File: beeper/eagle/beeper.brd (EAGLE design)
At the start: 27.6 x 41.9 mm, 32 parts, among them Q1 16MHz, T1 3904, U1 ATMEGA328P, U2 ATA6631

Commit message: Minor board tweaks. Work in progress.
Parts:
- moved R8 13.3 mm to (15.4, 10.7), turned to 180 degrees
- moved C4 13.3 mm to (24.7, 13.4), turned to 0 degrees
- moved T1 12.7 mm to (15.8, 6.73)
- moved C7 12.0 mm to (11.4, 18.4), turned to 90 degrees
- moved R1 7.54 mm to (19.6, 13.3)
- moved R10 6.35 mm to (15.2, 26.7)
- moved D1 6.29 mm to (15.7, 2.62), turned to 0 degrees
- moved C8 5.09 mm to (14.8, 21.2), turned to 270 degrees
- moved LED3 3.81 mm to (20.3, 3.81)
- moved R6 3.59 mm to (20.3, 32.4)
- moved R7 3.59 mm to (17.8, 32.4)
- moved U1 3.06 mm to (21.8, 20.4)
- moved U2 2.72 mm to (5.38, 17.8)
- moved C3 2.58 mm to (3.35, 22.9)
- moved JP2 2.54 mm to (24.1, 30.5), turned to 270 degrees
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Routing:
- net GND: track 0.00 -> 7.18 mm
- net N$1: track 0.00 -> 2.94 mm
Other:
- board size 27.6 x 41.9 mm -> 27.9 x 39.8 mm

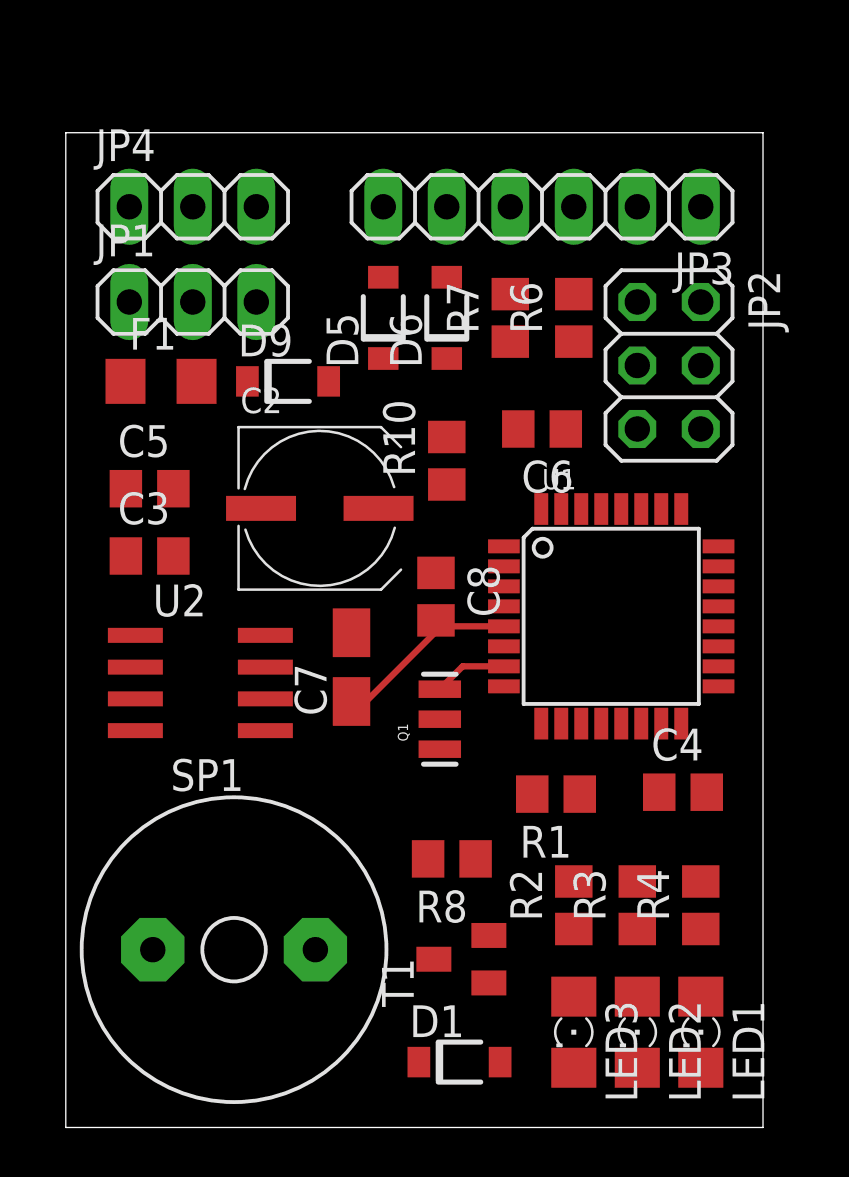
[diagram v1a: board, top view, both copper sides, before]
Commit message: First complete routing. Still needs TLC.
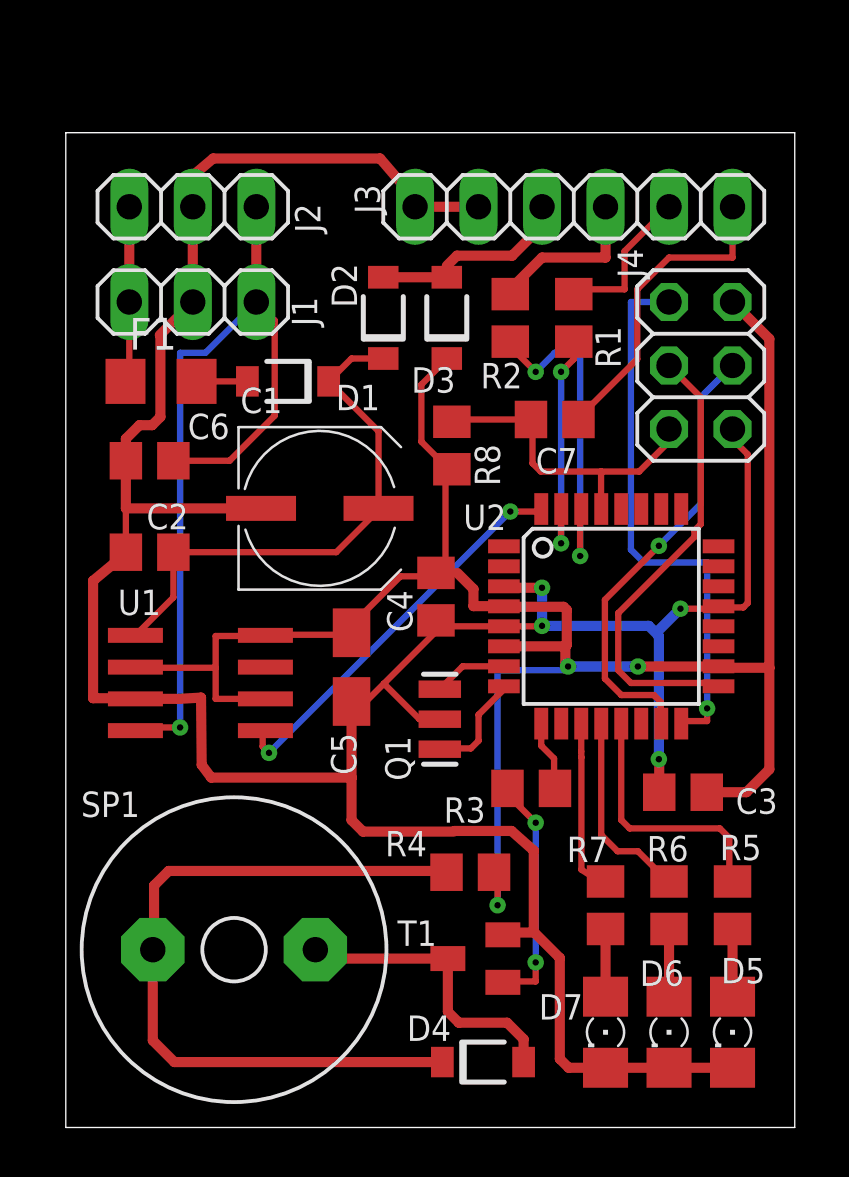
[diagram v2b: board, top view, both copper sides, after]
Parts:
- removed C8: 0.1uF, rcl:C0805
- removed D9: MBR0540, diode:SOD123FL
- removed JP2: ICSP, pinhead:2X03
- removed JP3: (no value), pinhead:1X06
- removed LED1, LED2: GREEN, led:1206
- removed LED3: RED, led:1206
- removed R10: 10k, rcl:R0805
- added C1: 22uF, rcl:UD-6,3X5,8_NICHICON
- added D2, D3: MBR0540, diode:SOD123FL
- added D4: MBR0560, diode:SOD123FL
- added D7: GREEN, led:1206
- added J3: (no value), pinhead:1X06
- added J4: ICSP, pinhead:2X03
- added R5: 3.3K, rcl:R0805
- C2: value 22uF -> 0.1uF; device rcl:UD-6,3X5,8_NICHICON -> rcl:C0805
- C3: value 220pF -> 0.1uF
- C5: value 0.1uF -> 10uF; device rcl:C0805 -> rcl:A/3216-18R
- C6: value 0.01uF -> 220pF
- C7: value 10uF -> 0.01uF; device rcl:A/3216-18R -> rcl:C0805
- D1: value MBR0560 -> MBR0540
- D5: value MBR0540 -> RED; device diode:SOD123FL -> led:1206
- D6: value MBR0540 -> GREEN; device diode:SOD123FL -> led:1206
- R1: value 5K -> 10k
- R2: value 3.3K -> 10k
- R3: value 470 -> 5K
- R4: value 470 -> 220
- R6, R7: value 10k -> 470
- R8: value 220 -> 10k
- U1: value ATMEGA328P -> ATA6631; device beeper:TQFP32-08 -> beeper:SO-08
- U2: value ATA6631 -> ATMEGA328P; device beeper:SO-08 -> beeper:TQFP32-08
- moved D5 31.8 mm to (26.7, 3.81), turned to 270 degrees
- moved D6 29.9 mm to (24.1, 3.81), turned to 270 degrees
- moved D1 28.1 mm to (8.89, 29.8), turned to 180 degrees
- moved R6 23.8 mm to (24.1, 8.89)
- moved R7 23.8 mm to (21.6, 8.89)
- moved R2 23.6 mm to (17.8, 32.4)
- moved C3 23.3 mm to (24.7, 13.4), turned to 180 degrees
- moved R1 19.1 mm to (20.3, 32.4), turned to 90 degrees
- moved U1 16.6 mm to (5.38, 17.8), turned to 270 degrees
- moved U2 16.6 mm to (21.8, 20.4), turned to 0 degrees
- moved R8 16.5 mm to (15.4, 27.3), turned to 270 degrees
- moved C6 15.7 mm to (3.35, 26.7)
- moved C7 12.8 mm to (19.6, 28.3), turned to 180 degrees
- moved C4 12.6 mm to (14.8, 21.2), turned to 270 degrees
- moved C5 10.8 mm to (11.4, 18.4), turned to 90 degrees
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- renumbered JP1 to J1, JP4 to J2
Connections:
- removed net N$1: Q1.3, U1.7
- removed net N$11: Q1.1, U1.8
- new net XTAL1: Q1.3, U2.7
- new net XTAL2: Q1.1, U2.8
- net +12V: now also C1.+, C2.1, D1.C, D2.C, U1.1; no longer C2.+, C5.1, D5.C, D9.C, U2.1
- net +5V: now also C3.1, C5.+, D3.C, J4.2, R4.2, U1.2, U1.8, U2.18, U2.4; no longer C7.+, C8.1, D6.C, JP2.2, R10.2, U1.18, U1.4, U2.2, U2.8
- net DTR: now also C7.1, J3.1; no longer C6.1, JP3.1
- net GND: now also C1.-, C2.2, C5.-, C6.2, D5.C, D6.C, D7.C, J3.5, J3.6, J4.6, U2.21, U2.5; no longer C2.-, C5.2, C7.-, C8.2, JP2.6, JP3.5, JP3.6, LED1.C, LED2.C, LED3.C, U1.21, U1.5
- net LIN: now also C6.1, U1.4; no longer C3.1, U2.4
- net LIN_RX: now also U1.5, U2.32; no longer U1.32, U2.5
- net N$14: now also R2.1, U2.30; no longer R7.1, U1.30
- net N$15: now also C7.2, J4.5, R8.1, U2.29; no longer C6.2, JP2.5, R10.1, U1.29
- net N$17: now also R3.1, U2.9; no longer R1.1, U1.9
- net N$19: now also R3.2; no longer R1.2
- net N$2: now also D7.A, R7.1; no longer LED1.A, R4.1
- net N$20: now also J4.4, U2.15; no longer JP2.4, U1.15
- net N$22: now also R1.1, U2.31; no longer R6.1, U1.31
- net N$25: now also J4.1, U2.16; no longer JP2.1, U1.16
- net N$28: now also J4.3, U2.17; no longer JP2.3, U1.17
- net N$3: now also D6.A, R6.1; no longer LED2.A, R3.1
- net N$30: now also D4.C, R4.1; no longer D1.C, R8.1
- net N$31: now also D4.A; no longer D1.A
- net N$4: now also D5.A, R5.1; no longer LED3.A, R2.1
- net N$6: now also D1.A; no longer D9.A
- net N$7: now also R5.2, U2.13; no longer R2.2, U1.13
- net N$8: now also R6.2, U2.12; no longer R3.2, U1.12
- net N$9: now also R7.2, U2.11; no longer R4.2, U1.11
- net RXI: now also J3.2, R1.2; no longer JP3.2, R6.2
- net S-5V: now also D2.A, D3.A, J3.4; no longer D5.A, D6.A, JP3.4
- net TXO: now also J3.3, R2.2; no longer JP3.3, R7.2
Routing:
- net GND: track 7.18 -> 121.8 mm, vias 0 -> 4
- net +5V: track 0.00 -> 83.5 mm, vias 0 -> 3
- net LIN: track 0.00 -> 34.2 mm, vias 0 -> 1
- net N$30: track 0.00 -> 30.1 mm
- net N$25: track 0.00 -> 22.2 mm, vias 0 -> 1
- net +12V: track 0.00 -> 21.4 mm
- net N$28: track 0.00 -> 18.3 mm
- net N$20: track 0.00 -> 18.1 mm, vias 0 -> 1
- net LIN_RX: track 0.00 -> 15.9 mm, vias 0 -> 2
- net N$14: track 0.00 -> 13.7 mm, vias 0 -> 2
- net N$15: track 0.00 -> 13.1 mm
- net DTR: track 0.00 -> 12.5 mm
- net N$31: track 0.00 -> 12.0 mm
- net N$7: track 0.00 -> 10.3 mm
- net N$22: track 0.00 -> 9.65 mm, vias 0 -> 2
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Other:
- board size 27.9 x 39.8 mm -> 29.2 x 39.8 mm

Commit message: Added heatsink copper below the LDO. General tweaks. Layout is complete. Need to verify and fix DRC's.
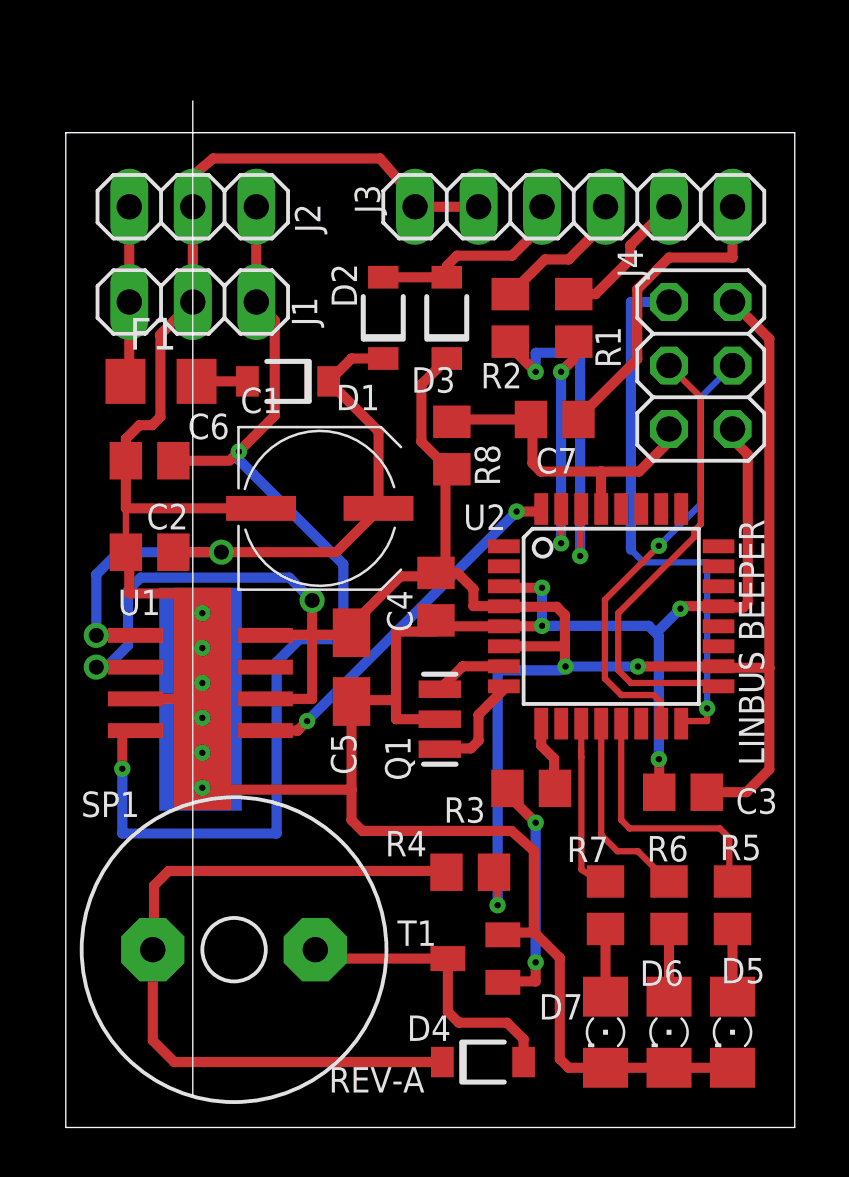
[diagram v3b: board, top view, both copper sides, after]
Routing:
- net N$1: track 0.00 -> 13.7 mm, vias 0 -> 6
- net +5V: track 83.5 -> 93.6 mm, vias 3 -> 5
- net LIN: track 34.2 -> 43.1 mm, vias 1 -> 2
- net +12V: track 21.4 -> 26.8 mm, vias 0 -> 2
- net GND: track 121.8 -> 126.1 mm
- net LIN_RX: track 15.9 -> 14.7 mm
- net TXO: track 6.56 -> 5.63 mm
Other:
- board size 29.2 x 39.8 mm -> 29.2 x 41.1 mm
- board text added: "LINBUS BEEPER"
- board text added: "REV-A"

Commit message: Updated PDF of board top view.
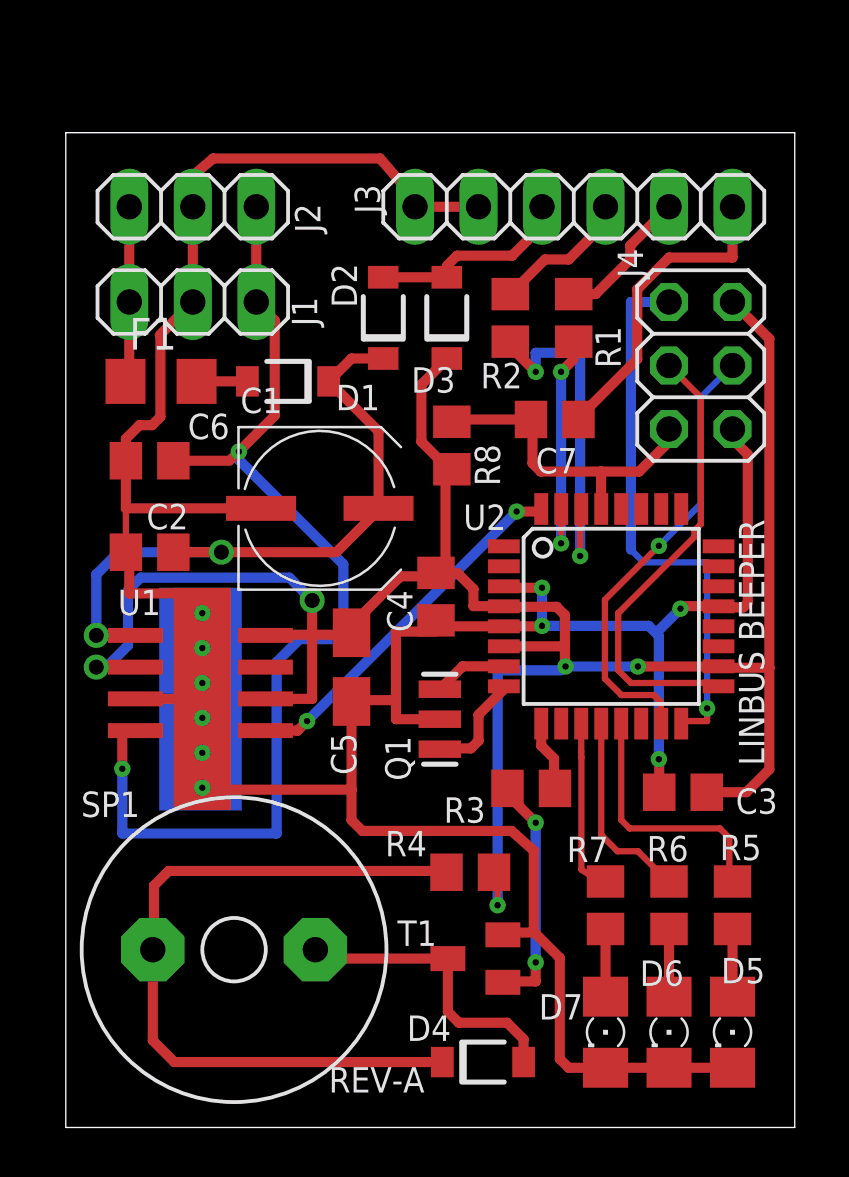
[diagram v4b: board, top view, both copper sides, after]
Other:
- board size 29.2 x 41.1 mm -> 29.2 x 39.8 mm
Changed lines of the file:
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@@
 <layer number="27" name="tValues" color="7" fill="1" visible="yes" active="yes"/>
 <layer number="28" name="bValues" color="7" fill="1" visible="yes" active="yes"/>
-<layer number="29" name="tStop" color="7" fill="3" visible="yes" active="yes"/>
-<layer number="30" name="bStop" color="7" fill="6" visible="yes" active="yes"/>
-<layer number="31" name="tCream" color="7" fill="4" visible="yes" active="yes"/>
-<layer number="32" name="bCream" color="7" fill="5" visible="yes" active="yes"/>
-<layer number="33" name="tFinish" color="6" fill="3" visible="yes" active="yes"/>
-<layer number="34" name="bFinish" color="6" fill="6" visible="yes" active="yes"/>
+<layer number="29" name="tStop" color="7" fill="3" visible="no" active="yes"/>
+<layer number="30" name="bStop" color="7" fill="6" visible="no" active="yes"/>
+<layer number="31" name="tCream" color="7" fill="4" visible="no" active="yes"/>
+<layer number="32" name="bCream" color="7" fill="5" visible="no" active="yes"/>
+<layer number="33" name="tFinish" color="6" fill="3" visible="no" active="yes"/>
+<layer number="34" name="bFinish" color="6" fill="6" visible="no" active="yes"/>
 <layer number="35" name="tGlue" color="7" fill="4" visible="yes" active="yes"/>
 <layer number="36" name="bGlue" color="7" fill="5" visible="yes" active="yes"/>
@@
 <layer number="103" name="tMap" color="7" fill="1" visible="yes" active="yes"/>
 <layer number="104" name="Name" color="7" fill="1" visible="yes" active="yes"/>
-<layer number="105" name="tPlate" color="7" fill="1" visible="yes" active="yes"/>
-<layer number="106" name="bPlate" color="7" fill="1" visible="yes" active="yes"/>
+<layer number="105" name="tPlate" color="7" fill="1" visible="no" active="yes"/>
+<layer number="106" name="bPlate" color="7" fill="1" visible="no" active="yes"/>
 <layer number="107" name="Crop" color="7" fill="1" visible="yes" active="yes"/>
 <layer number="116" name="Patch_BOT" color="9" fill="4" visible="yes" active="yes"/>
@@
 <rectangle x1="4.318" y1="12.7" x2="6.604" y2="21.59" layer="1"/>
 <rectangle x1="3.7338" y1="12.6746" x2="7.0358" y2="21.59" layer="16"/>
-<wire x1="5.08" y1="41.0618" x2="5.08" y2="1.27" width="0" layer="20"/>
 <text x="27.94" y="14.478" size="1.016" layer="21" rot="R90">LINBUS BEEPER</text>
 <text x="14.351" y="2.413" size="1.016" layer="21" rot="R180">REV-A</text>

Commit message: Increased min dril to 12mil to comply with PCB house requirements.
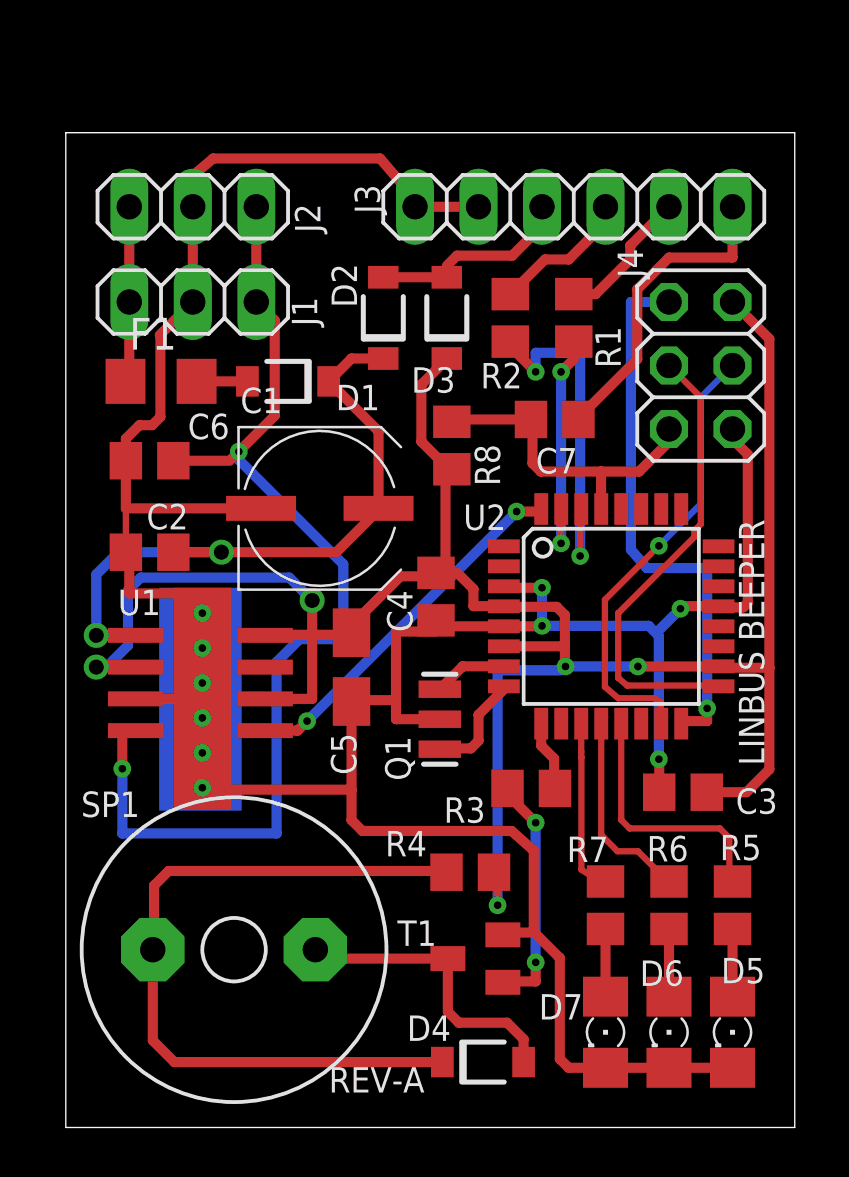
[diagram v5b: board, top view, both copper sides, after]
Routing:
- net N$1: track 13.7 -> 2.77 mm, vias 6 -> 2
- net GND: track 126.1 -> 122.3 mm
- net N$5: track 0.00 -> 1.50 mm, vias 0 -> 2

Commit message: Board layout tweaked and verified.
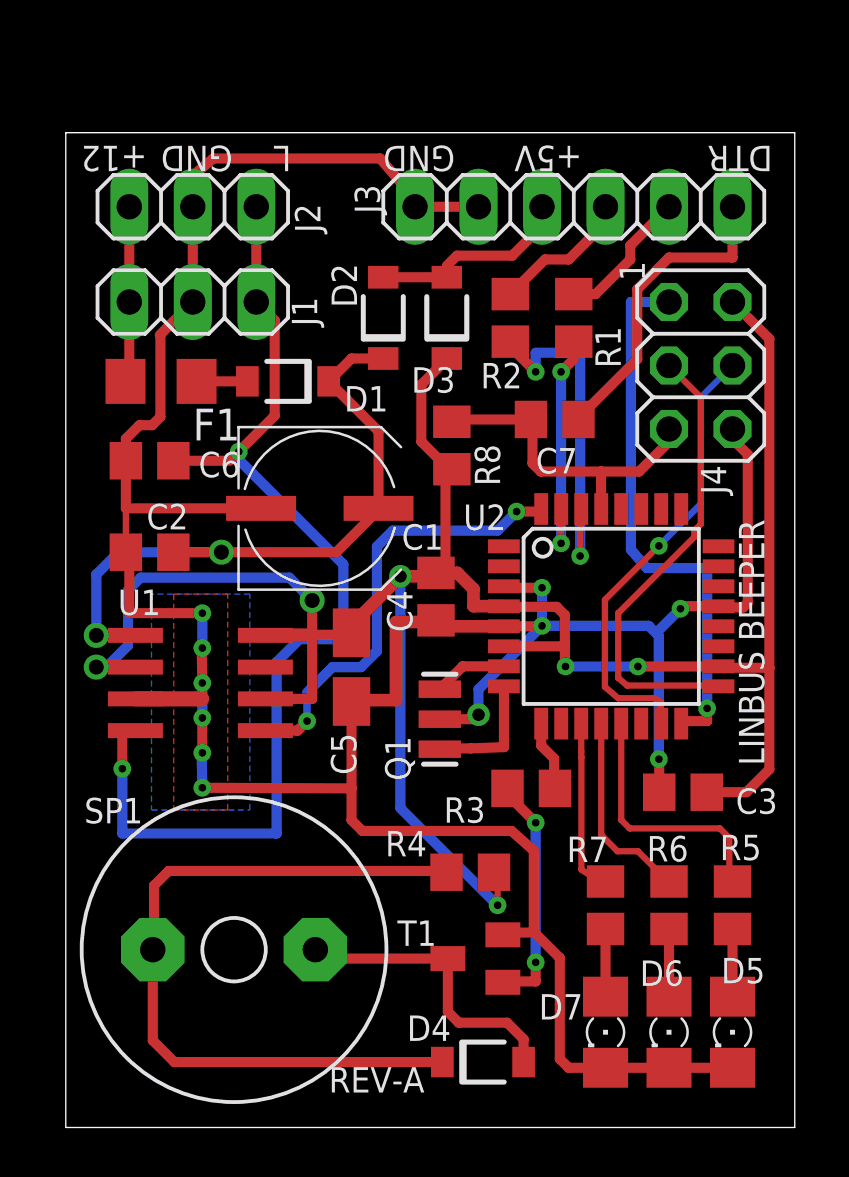
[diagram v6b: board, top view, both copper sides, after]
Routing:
- net GND: track 122.3 -> 131.0 mm, vias 4 -> 11
- net LIN_RX: track 14.7 -> 17.8 mm
- net +5V: track 93.6 -> 96.4 mm, vias 5 -> 6
- net N$1: track 2.77 -> 0.00 mm, vias 2 -> 0
- net N$5: track 1.50 -> 0.00 mm, vias 2 -> 0
- net XTAL2: track 4.61 -> 5.34 mm
- added copper zone on layer 1, net GND
- added copper zone on layer 16, net GND
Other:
- board text added: "+12"
- board text added: "+5V"
- board text added: "1"
- board text added: "DTR"
- board text added: "GND"
- board text added: "L"
